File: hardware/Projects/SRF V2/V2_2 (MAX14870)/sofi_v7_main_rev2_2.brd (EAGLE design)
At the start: 59.7 x 65.7 mm, 82 parts

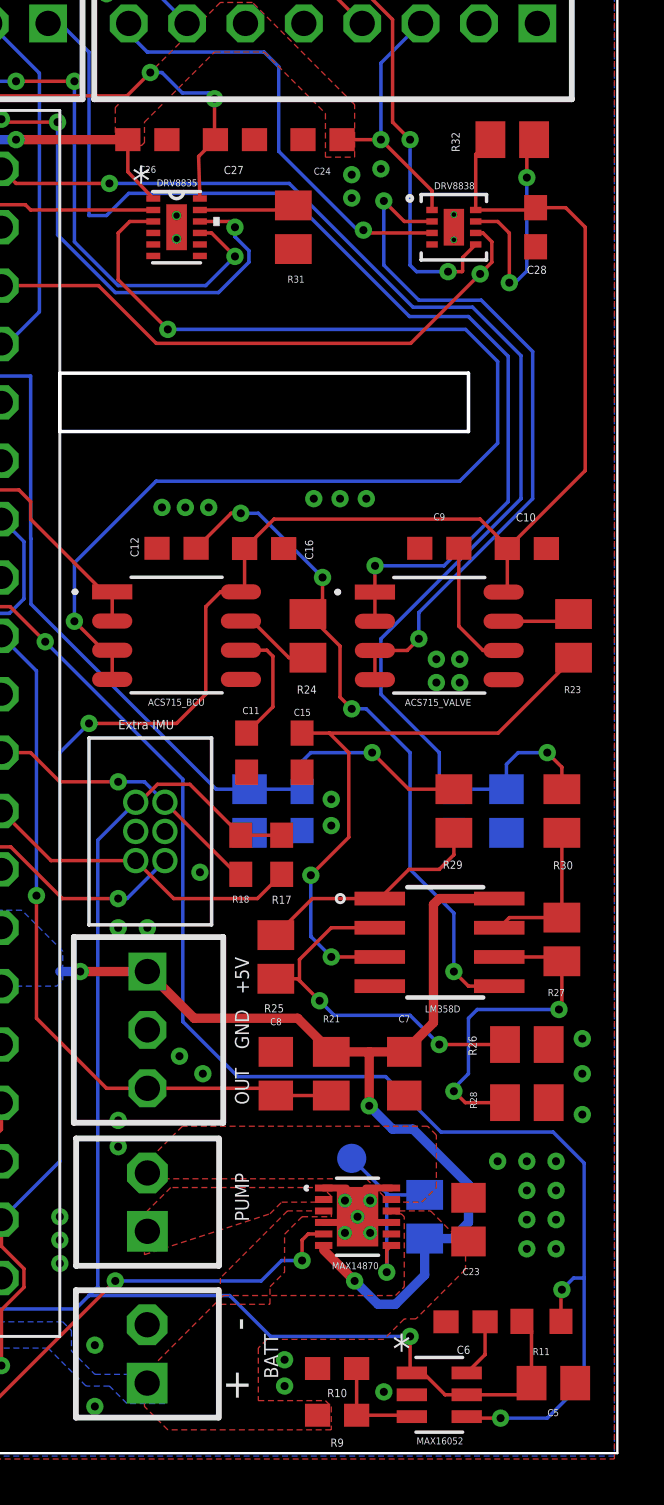
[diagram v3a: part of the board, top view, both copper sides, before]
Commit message: extended motor driver pads, removed top thermals on power module thermal vias
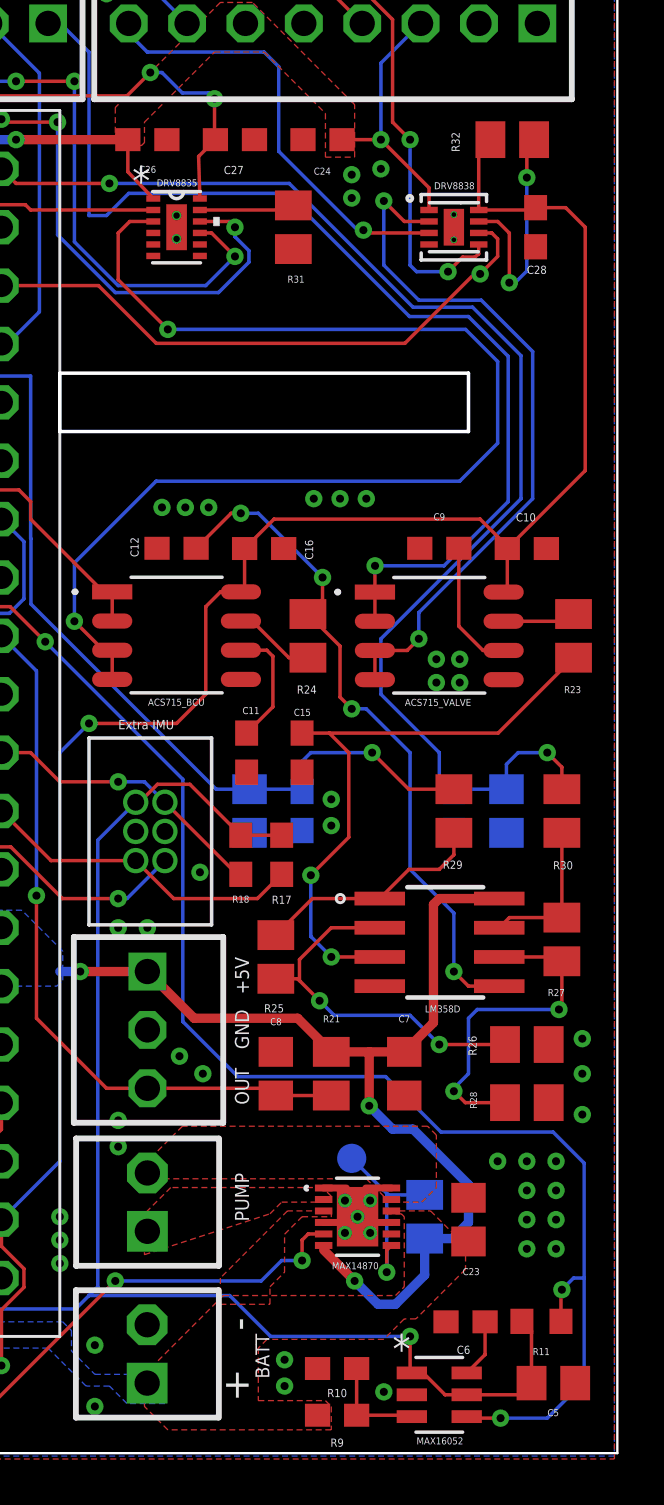
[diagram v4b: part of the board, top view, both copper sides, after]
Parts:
- DRV8838: value DRV8838DSGTDSG8_P9X1P6_THERMAL -> DRV8838DSGTDSG8_P9X1P6_THERMAL_EXTENDED; device DRV8838:DSG8_P9X1P6_THERMAL -> DRV8838:DSG8_P9X1P6_THERMAL_EXTENDED
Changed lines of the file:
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@@
 <attribute name="VALUE" x="2.667" y="10.16" size="1.27" layer="28" ratio="10" rot="MR90"/>
 </element>
-<element name="DRV8838" library="DRV8838" package="DSG8_P9X1P6_THERMAL" value="DRV8838DSGTDSG8_P9X1P6_THERMAL" x="56.515" y="55.88" smashed="yes">
+<element name="DRV8838" library="DRV8838" package="DSG8_P9X1P6_THERMAL_EXTENDED" value="DRV8838DSGTDSG8_P9X1P6_THERMAL_EXTENDED" x="56.515" y="55.88" smashed="yes">
 <attribute name="NAME" x="55.6514" y="57.531" size="0.3048" layer="25" ratio="6" rot="SR0"/>
 </element>
@@
 </element>
 <element name="BATT" library="2pos_block_terminal" package="2POS_BLOCK_NOSTANDS" value="2POS_BLOCK2POS_BLOCK_NOSTANDS" x="44.44" y="6.858" smashed="yes" rot="R90">
-<attribute name="NAME" x="48.26" y="7.737" size="0.6096" layer="25" ratio="18" rot="R270"/>
+<attribute name="NAME" x="47.879" y="7.737" size="0.6096" layer="25" ratio="18" rot="R270"/>
 </element>
 <element name="HALL" library="3pos_block_terminal" package="3POS_TERMINAL" value="3POS_TERMINAL" x="43.18" y="22.225" smashed="yes" rot="R270"/>
@@
 <wire x1="47.41" y1="41.9" x2="47.41" y2="40.175" width="0.1524" layer="1"/>
 <wire x1="47.41" y1="40.175" x2="47.25" y2="40.015" width="0.1524" layer="1"/>
-<wire x1="57.465" y1="56.63" x2="57.465" y2="59.05" width="0.1524" layer="1"/>
-<wire x1="57.465" y1="59.05" x2="58.105" y2="59.69" width="0.1524" layer="1"/>
 <wire x1="39.37" y1="33.02" x2="40.64" y2="34.29" width="0.1524" layer="16"/>
 <via x="40.64" y="34.29" extent="1-16" drill="0.35"/>
@@
 <wire x1="62.23" y1="55.88" x2="62.23" y2="45.29" width="0.1524" layer="1"/>
 <wire x1="62.23" y1="45.29" x2="58.84" y2="41.9" width="0.1524" layer="1"/>
-<wire x1="57.465" y1="56.63" x2="59.971" y2="56.63" width="0.1524" layer="1"/>
+<wire x1="57.596" y1="56.63" x2="59.971" y2="56.63" width="0.1524" layer="1"/>
 <wire x1="59.971" y1="56.63" x2="60.071" y2="56.73" width="0.1524" layer="1"/>
 <wire x1="60.071" y1="56.73" x2="61.38" y2="56.73" width="0.1524" layer="1"/>
@@
 <vertex x="29.591" y="26.797"/>
 </polygon>
+<wire x1="57.596" y1="56.63" x2="57.596" y2="59.181" width="0.1524" layer="1"/>
+<wire x1="57.596" y1="59.181" x2="58.105" y2="59.69" width="0.1524" layer="1"/>
 </signal>
 <signal name="MBED_RST">
@@
 <vertex x="20.193" y="24.13"/>
 <vertex x="20.32" y="26.416"/>
-<vertex x="20.32" y="26.416"/>
 <vertex x="20.574" y="26.67"/>
 <vertex x="20.574" y="27.94"/>
@@
 <wire x1="53.34" y1="59.69" x2="53.34" y2="63.02025" width="0.1524" layer="16"/>
 <wire x1="53.34" y1="63.02025" x2="55.067153125" y2="64.747403125" width="0.1524" layer="16"/>
-<wire x1="55.565" y1="56.63" x2="55.565" y2="57.465" width="0.1524" layer="1"/>
-<wire x1="55.565" y1="57.465" x2="53.34" y2="59.69" width="0.1524" layer="1"/>
 <polygon width="0.1524" layer="16" isolate="0.254" thermals="no">
 <vertex x="28.829" y="47.752"/>
@@
 <vertex x="41.783" y="61.087"/>
 </polygon>
+<wire x1="55.434" y1="56.63" x2="55.434" y2="57.596" width="0.1524" layer="1"/>
+<wire x1="55.434" y1="57.596" x2="53.34" y2="59.69" width="0.1524" layer="1"/>
 </signal>
 <signal name="N$7">
@@
 <vertex x="43.053" y="12.954"/>
 <vertex x="43.053" y="11.176"/>
-<vertex x="48.514" y="12.954"/>
 <vertex x="48.514" y="12.954"/>
 <vertex x="49.022" y="13.462"/>
@@
 <wire x1="59.944" y1="44.069" x2="54.991" y2="39.116" width="0.1524" layer="16"/>
 <wire x1="53.467" y1="57.023" x2="54.36" y2="56.13" width="0.1524" layer="1"/>
-<wire x1="54.36" y1="56.13" x2="55.565" y2="56.13" width="0.1524" layer="1"/>
+<wire x1="54.36" y1="56.13" x2="55.434" y2="56.13" width="0.1524" layer="1"/>
 <wire x1="54.991" y1="52.705" x2="57.70805625" y2="52.705" width="0.1524" layer="16"/>
 <wire x1="57.70805625" y1="52.705" x2="59.944" y2="50.46905625" width="0.1524" layer="16"/>
@@
 <contactref element="DRV8838" pad="3"/>
 <contactref element="U$4" pad="8"/>
-<wire x1="55.565" y1="55.63" x2="52.701" y2="55.63" width="0.1524" layer="1"/>
+<wire x1="55.434" y1="55.63" x2="52.701" y2="55.63" width="0.1524" layer="1"/>
 <wire x1="52.701" y1="55.63" x2="52.578" y2="55.753" width="0.1524" layer="1"/>
 <via x="52.578" y="55.753" extent="1-16" drill="0.35"/>
@@
 <wire x1="29.845" y1="62.103" x2="29.845" y2="65.532" width="0.1524" layer="1"/>
 <wire x1="31.377" y1="67.064" x2="29.845" y2="65.532" width="0.1524" layer="1"/>
-<wire x1="57.465" y1="55.13" x2="56.896" y2="54.561" width="0.1524" layer="1"/>
-<wire x1="56.896" y1="54.561" x2="56.896" y2="53.975" width="0.1524" layer="1"/>
-<wire x1="56.896" y1="53.975" x2="56.8678" y2="53.9468" width="0.1524" layer="1"/>
-<wire x1="56.8678" y1="53.9468" x2="56.261" y2="53.9468" width="0.1524" layer="1"/>
+<wire x1="57.596" y1="55.13" x2="57.596" y2="54.71706875" width="0.1524" layer="1"/>
+<wire x1="57.596" y1="54.71706875" x2="57.429590625" y2="54.5818" width="0.1524" layer="1"/>
+<wire x1="57.429590625" y1="54.5818" x2="56.896" y2="54.5818" width="0.1524" layer="1"/>
+<wire x1="56.896" y1="54.5818" x2="56.261" y2="53.9468" width="0.1524" layer="1"/>
 <via x="56.261" y="53.9468" extent="1-16" drill="0.35"/>
 <wire x1="56.261" y1="53.9468" x2="54.8922" y2="53.9468" width="0.1524" layer="16"/>
@@
 <contactref element="DRV8838" pad="6"/>
 <contactref element="MBED" pad="18"/>
-<wire x1="57.465" y1="55.63" x2="57.781" y2="55.63" width="0.1524" layer="1"/>
-<wire x1="57.781" y1="55.63" x2="58.166" y2="55.245" width="0.1524" layer="1"/>
-<wire x1="58.166" y1="55.245" x2="58.166" y2="54.356" width="0.1524" layer="1"/>
-<wire x1="58.166" y1="54.356" x2="57.658" y2="53.848" width="0.1524" layer="1"/>
+<wire x1="57.596" y1="55.63" x2="58.162" y2="55.63" width="0.1524" layer="1"/>
+<wire x1="58.162" y1="55.63" x2="58.42" y2="55.372" width="0.1524" layer="1"/>
+<wire x1="58.42" y1="55.372" x2="58.42" y2="54.61" width="0.1524" layer="1"/>
+<wire x1="58.42" y1="54.61" x2="57.658" y2="53.848" width="0.1524" layer="1"/>
 <via x="57.658" y="53.848" extent="1-16" drill="0.35"/>
 <wire x1="36.83" y1="53.34" x2="41.05185" y2="53.34" width="0.1524" layer="1"/>
 <wire x1="41.05185" y1="53.34" x2="43.56365" y2="50.8282" width="0.1524" layer="1"/>
-<wire x1="43.56365" y1="50.8282" x2="54.6382" y2="50.8282" width="0.1524" layer="1"/>
-<wire x1="54.6382" y1="50.8282" x2="57.658" y2="53.848" width="0.1524" layer="1"/>
+<wire x1="43.56365" y1="50.8282" x2="54.3842" y2="50.8282" width="0.1524" layer="1"/>
+<wire x1="57.404" y1="53.848" x2="57.658" y2="53.848" width="0.1524" layer="1"/>
+<wire x1="57.404" y1="53.848" x2="54.3842" y2="50.8282" width="0.1524" layer="1"/>
 </signal>
 <signal name="N$42">
@@
 <wire x1="59.69" y1="58.039" x2="59.69" y2="59.375" width="0.1524" layer="1"/>
 <wire x1="59.69" y1="59.375" x2="60.005" y2="59.69" width="0.1524" layer="1"/>
-<wire x1="57.465" y1="56.13" x2="58.424" y2="56.13" width="0.1524" layer="1"/>
+<wire x1="57.596" y1="56.13" x2="58.424" y2="56.13" width="0.1524" layer="1"/>
 <wire x1="58.424" y1="56.13" x2="58.928" y2="55.626" width="0.1524" layer="1"/>
 <wire x1="58.928" y1="55.626" x2="58.928" y2="53.467" width="0.1524" layer="1"/>

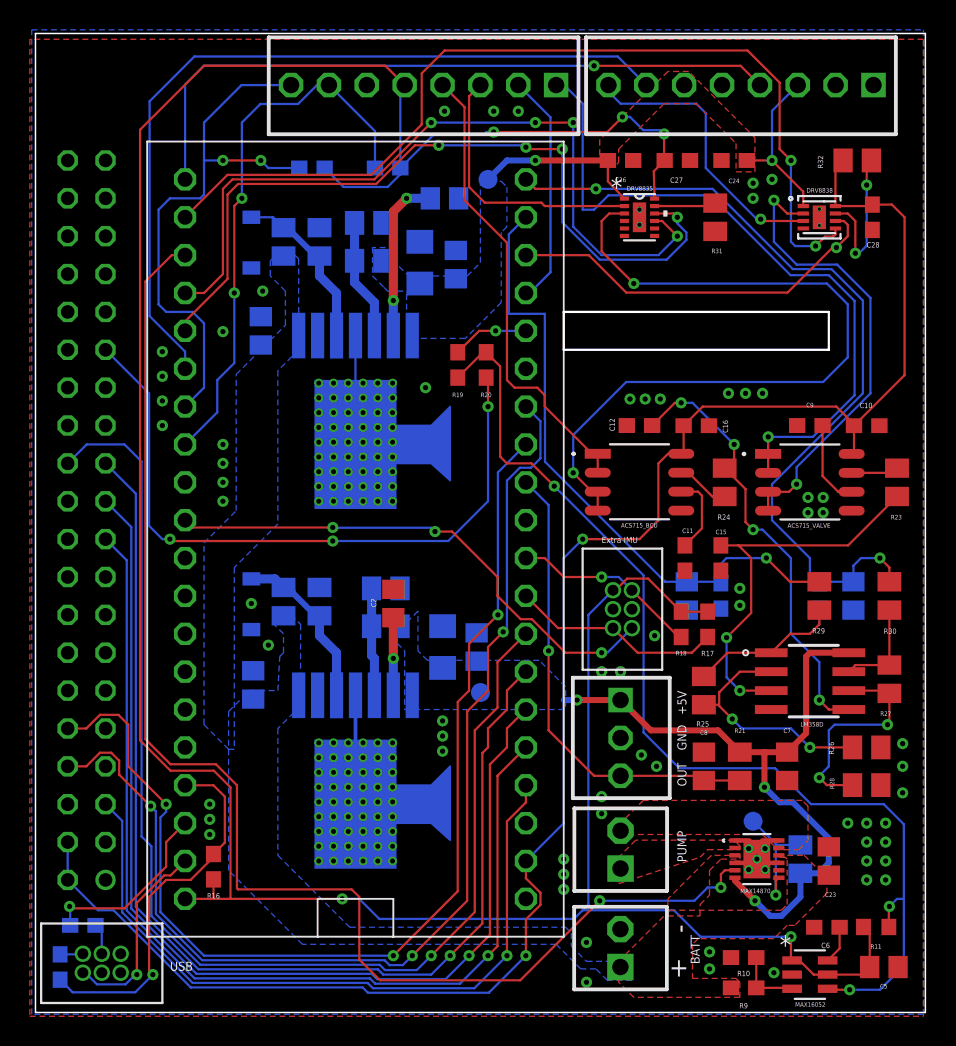
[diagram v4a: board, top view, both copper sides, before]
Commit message: defined corner radius around camera cable cut-out, widened valve & bcu motor output traces for safety, rearranged some polygons
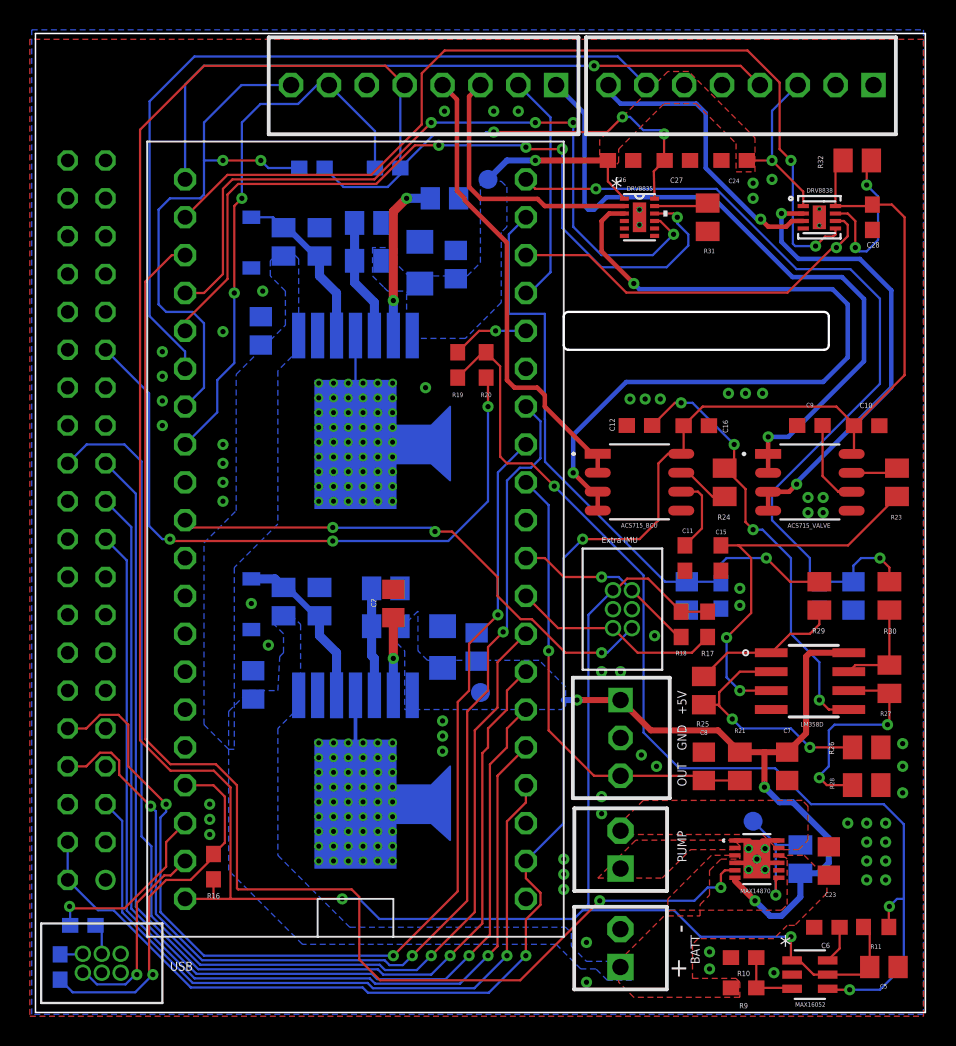
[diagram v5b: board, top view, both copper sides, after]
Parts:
- moved R31 0.51 mm to (49.0, 55.9)
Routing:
- net BCU_CURRENT: track 56.0 -> 57.7 mm
- net BCU_PWM_1: track 52.6 -> 53.6 mm
- net VALVE_MOTOR_V2: track 46.7 -> 46.0 mm
- net N$42: track 10.5 -> 11.0 mm
- net N$34: track 4.15 -> 3.64 mm
- net BCU_PWM_2: track 51.4 -> 50.8 mm
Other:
- outline, holes or cut-outs redrawn
